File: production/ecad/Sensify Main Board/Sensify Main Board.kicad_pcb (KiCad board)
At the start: 4 copper layers, 150 parts, among them J1 1-2834011-3, J2 1-2834011-2, J3 1332645, J4 0532611271, J5 Screw_Terminal_01x08, J6 Conn_01x02_Socket, J7 Conn_01x02_Socket, J8 Conn_01x02_Socket, J9 Conn_01x02_Socket, Q1 2N700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

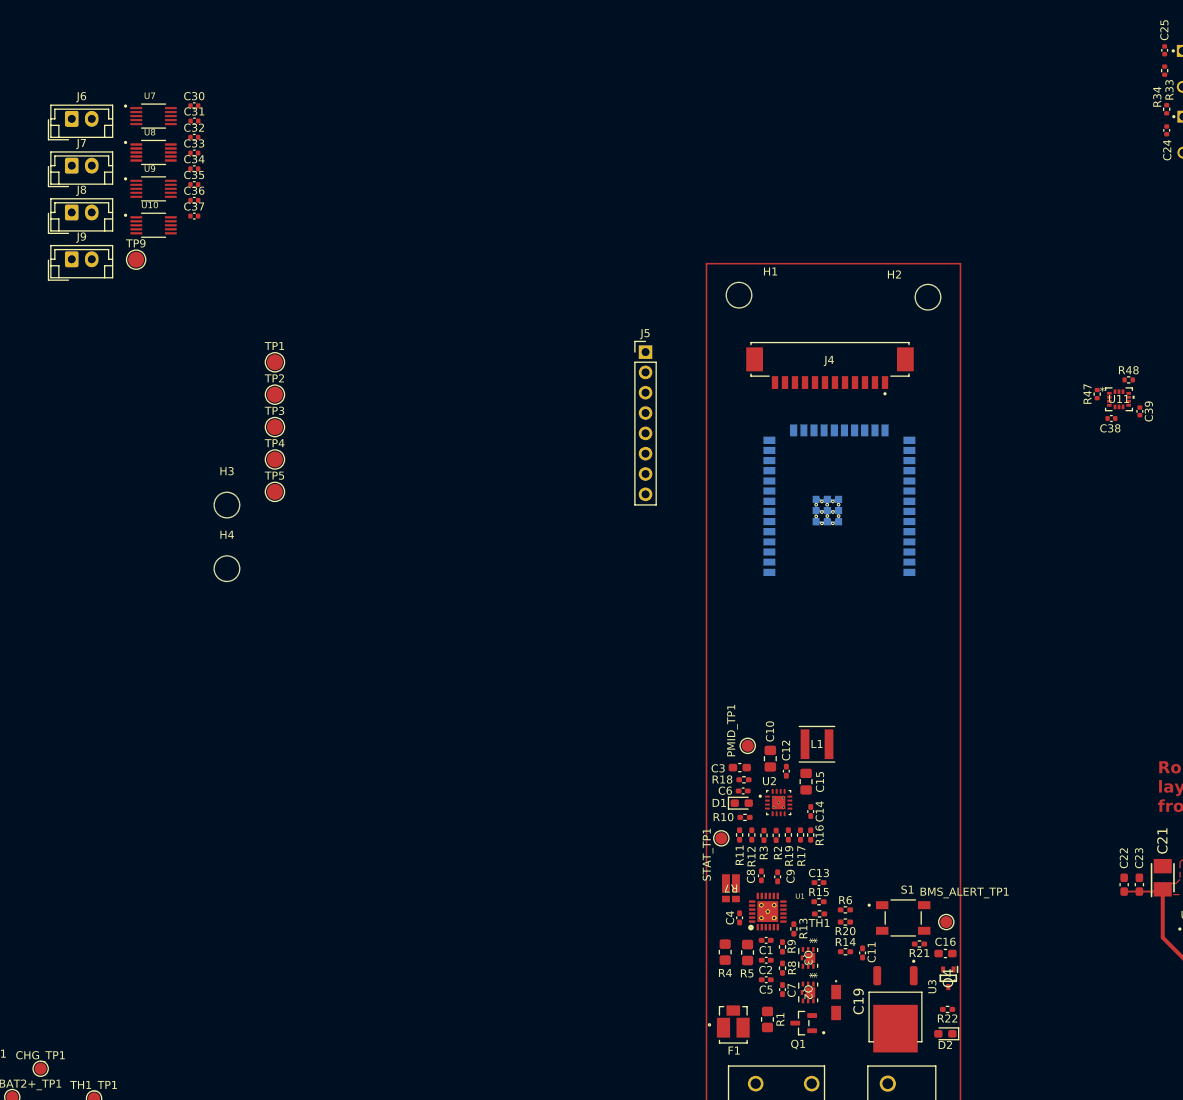
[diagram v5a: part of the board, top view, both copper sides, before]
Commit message: main board
routed haptics, modified 3.3V supply
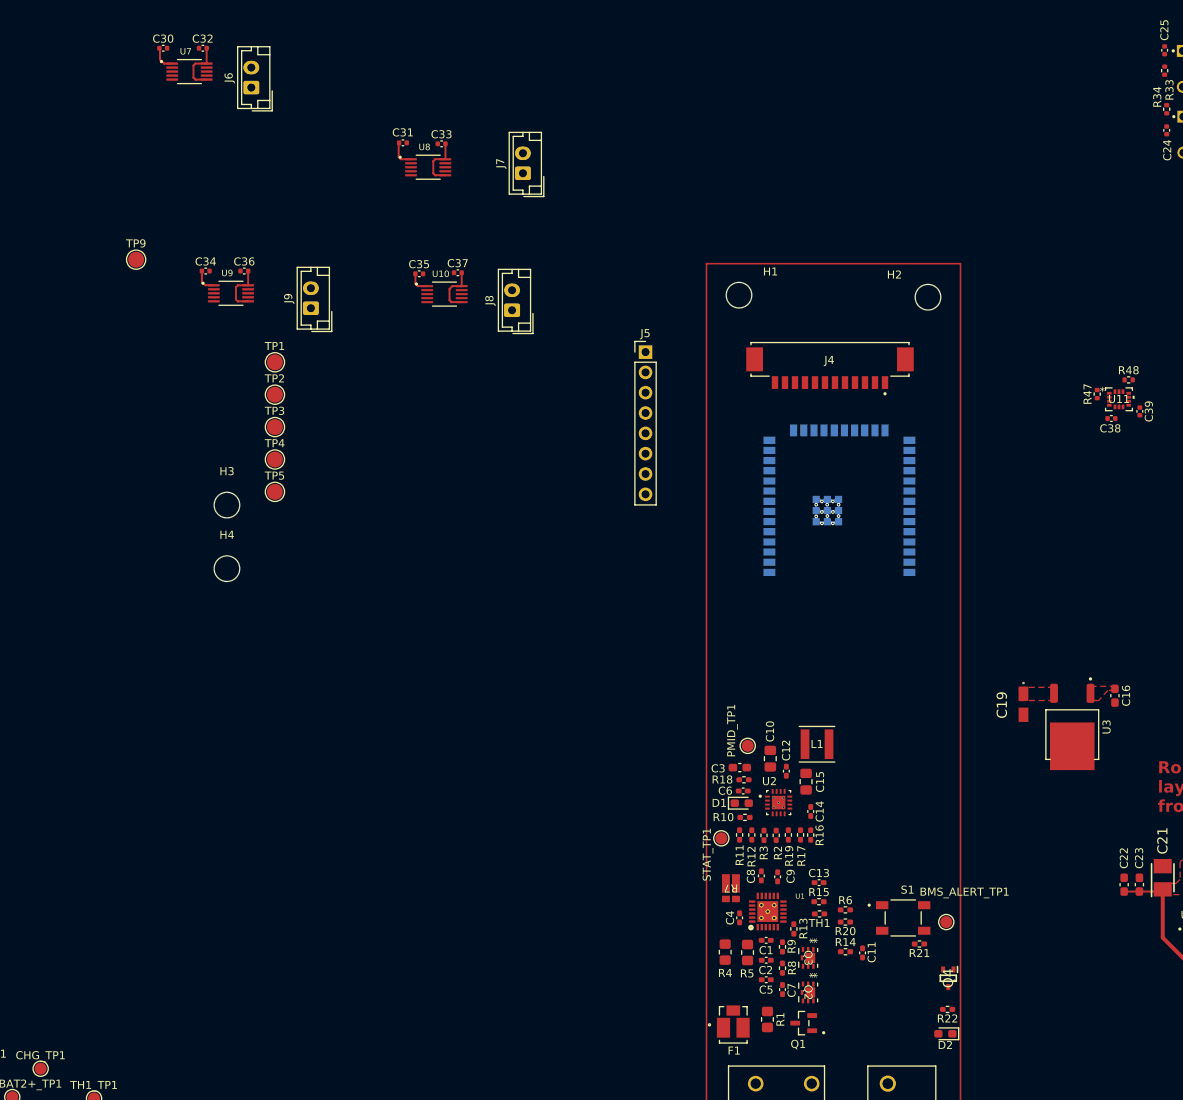
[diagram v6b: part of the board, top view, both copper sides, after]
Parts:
- moved J7 56.4 mm to (104.6, 58.3), turned to 90 degrees
- moved J8 56.4 mm to (103.2, 75.4), turned to 90 degrees
- moved C19 44.0 mm to (167.1, 124.7)
- moved U3 41.6 mm to (173.2, 127.5)
- moved C16 38.6 mm to (178.6, 123.6), turned to -90 degrees
- moved U10 37.4 mm to (94.8, 73.4)
- moved U8 34.4 mm to (92.7, 57.5)
- moved C37 33.7 mm to (96.4, 70.7)
- moved C33 30.9 mm to (94.4, 54.6)
- moved J9 30.5 mm to (78.1, 75.2), turned to 90 degrees
- moved C35 30.3 mm to (91.6, 70.9)
- moved C31 26.2 mm to (89.6, 54.5)
- moved J6 22.8 mm to (70.6, 47.6), turned to 90 degrees
- moved U9 16.2 mm to (68.1, 73.3)
- moved C34 12.9 mm to (64.9, 70.5)
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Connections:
- C30 pad 2: Earth -> GND
- C31 pad 2: Earth -> GND
- C32 pad 1: Earth -> GND
- C33 pad 1: Earth -> GND
- C34 pad 2: Earth -> GND
- C35 pad 2: Earth -> GND
- C36 pad 1: Earth -> GND
- C37 pad 1: Earth -> GND
- U10 pad 4: Earth -> GND
- U10 pad 8: Earth -> GND
- U7 pad 4: Earth -> GND
- U7 pad 8: Earth -> GND
- U8 pad 4: Earth -> GND
- U8 pad 8: Earth -> GND
- U9 pad 4: Earth -> GND
- U9 pad 8: Earth -> GND
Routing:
- net +5V: track 15.6 -> 42.2 mm
- net Net-(U8-REG): track 0.00 -> 3.46 mm
- net Net-(U7-REG): track 0.00 -> 3.17 mm
- net Net-(U9-REG): track 0.00 -> 3.00 mm
- net Net-(U10-REG): track 0.00 -> 2.82 mm
- added copper zone on F.Cu, net +3V3

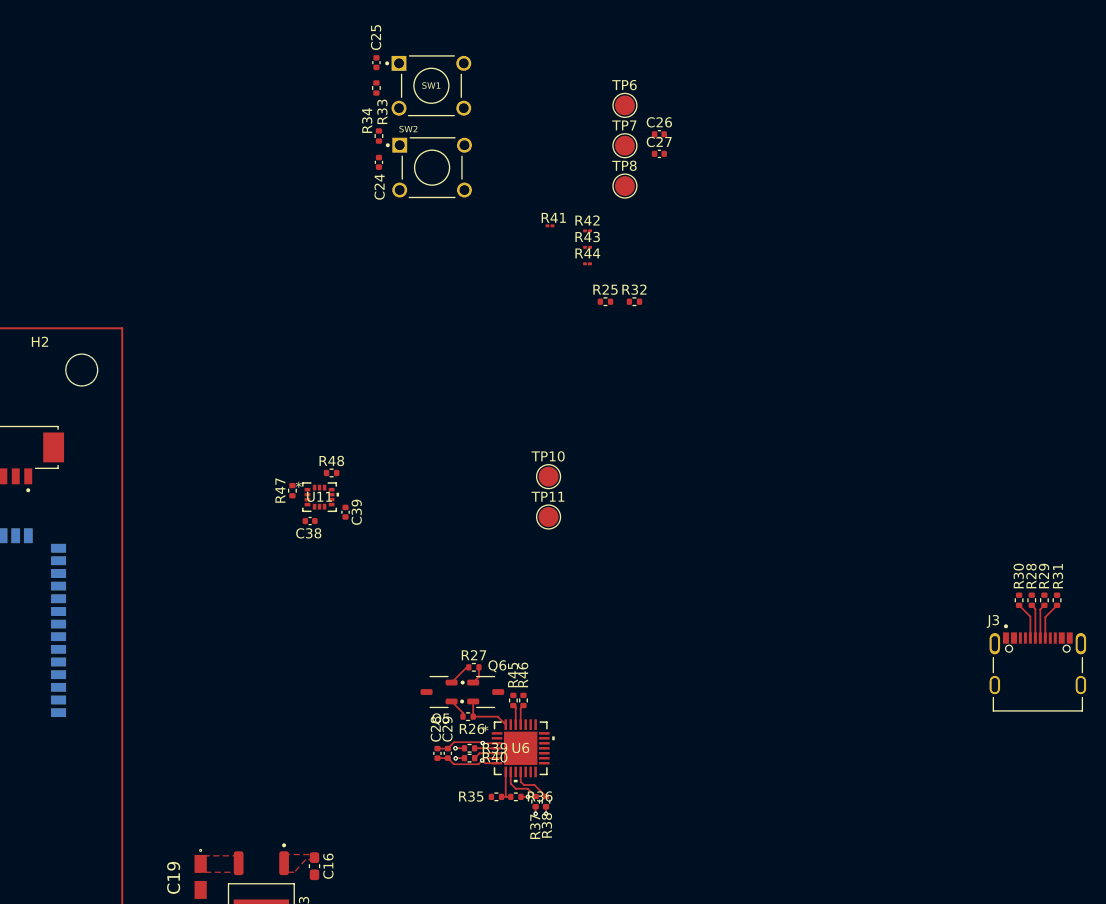
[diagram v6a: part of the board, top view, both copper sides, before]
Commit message: Finished USB to UART Routing
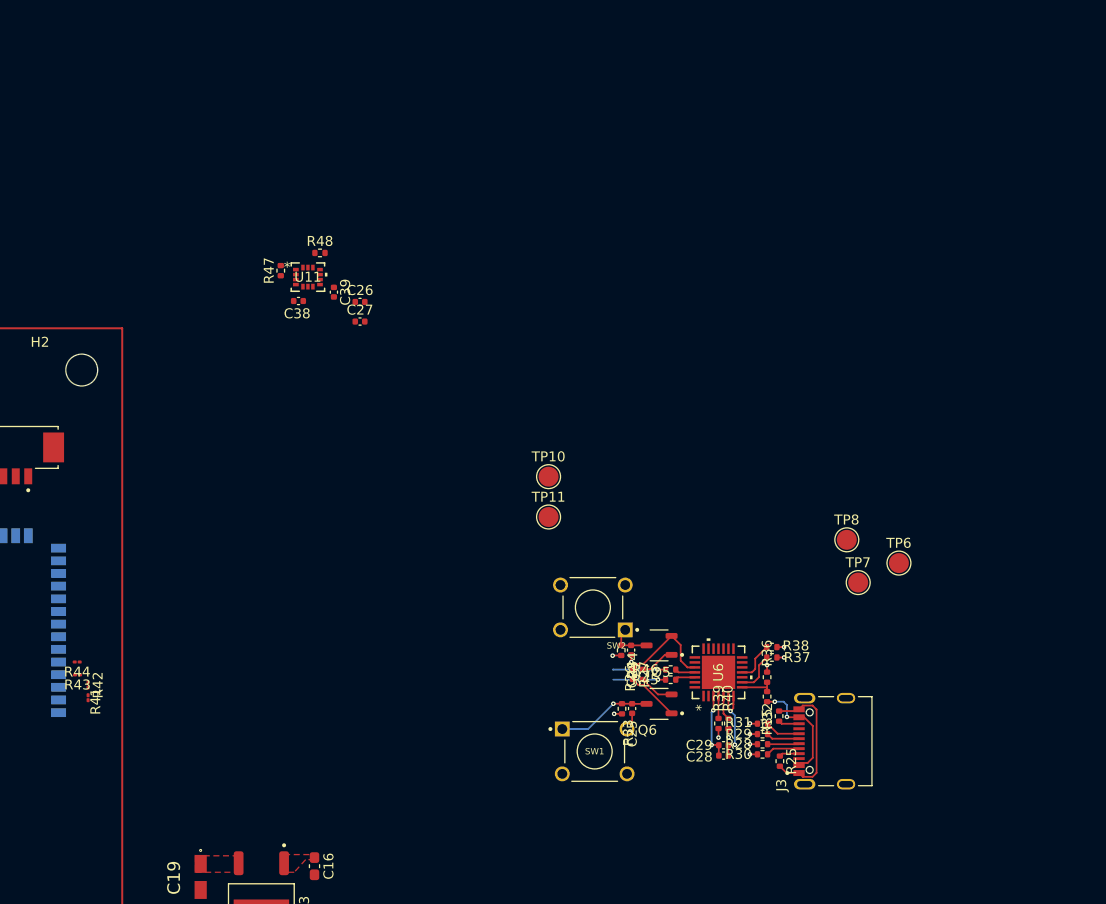
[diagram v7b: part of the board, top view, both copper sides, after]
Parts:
- moved C25 69.7 mm to (210.4, 107.8), turned to -90 degrees
- moved SW1 68.8 mm to (206.7, 112.1)
- moved R42 67.8 mm to (155.8, 105.4), turned to -90 degrees
- moved R33 67.0 mm to (209.4, 107.8)
- moved R43 66.8 mm to (154.8, 104.4), turned to 180 degrees
- moved R41 66.3 mm to (155.8, 106.7), turned to -90 degrees
- moved R44 65.0 mm to (154.7, 103.1), turned to 180 degrees
- moved R34 57.1 mm to (209.4, 101.9), turned to 90 degrees
- moved C24 55.1 mm to (210.3, 101.9)
- moved TP6 53.6 mm to (237.2, 93.2)
- moved TP7 49.7 mm to (233.1, 95.1)
- moved R25 49.3 mm to (225.3, 113.1), turned to -90 degrees
- moved SW2 47.0 mm to (206.5, 97.6), turned to 180 degrees
- moved R32 44.1 mm to (225.2, 108.5), turned to 90 degrees
- moved TP8 41.9 mm to (232.0, 90.8)
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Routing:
- net GND: track 25.7 -> 43.5 mm, vias 15 -> 17
- net FLASHING_VBUS_5V: track 0.00 -> 11.2 mm, vias 0 -> 2
- net IO0: track 0.00 -> 9.52 mm, vias 0 -> 1
- net RTS: track 2.36 -> 9.83 mm
- net UART_RXD: track 0.00 -> 5.28 mm, vias 0 -> 1
- net UART_TXD: track 0.00 -> 5.25 mm, vias 0 -> 1
- net EN: track 0.00 -> 4.27 mm
- net Net-(Q6-Pad1): track 1.77 -> 5.30 mm
- net Net-(J3-CC2): track 0.00 -> 2.11 mm
- net +3V3: track 8.80 -> 10.9 mm, vias 2 -> 5
- net Net-(J3-CC1): track 0.00 -> 2.03 mm
- net DTR: track 5.13 -> 3.49 mm
- net USB_D+: track 0.91 -> 2.44 mm, vias 1 -> 3
- net USB_D-: track 0.90 -> 2.41 mm, vias 1 -> 3
- net Net-(Q5-Pad1): track 2.00 -> 3.47 mm

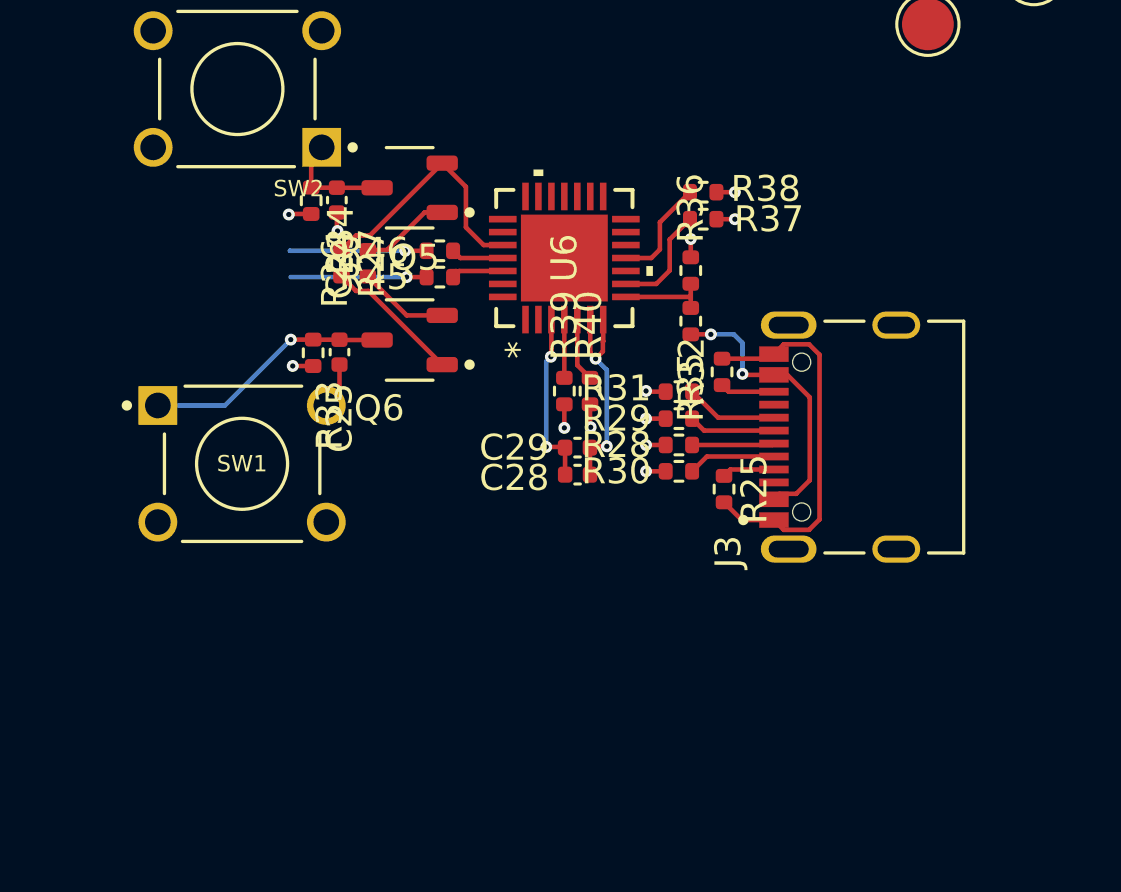
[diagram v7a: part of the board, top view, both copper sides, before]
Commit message: Deleted routing for USB to UART to allow more flexibility
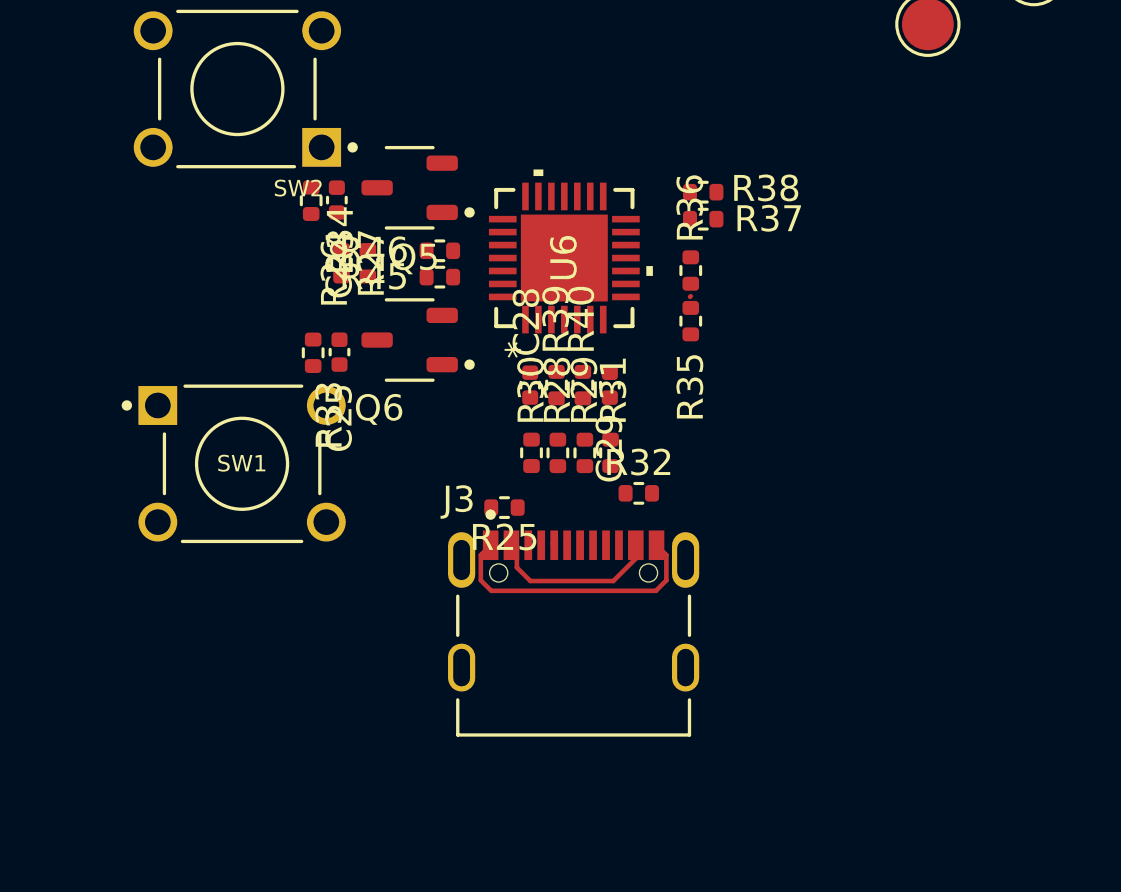
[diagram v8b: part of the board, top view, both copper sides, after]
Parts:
- moved J3 20.7 mm to (215.0, 122.5), turned to 0 degrees
- moved R25 8.50 mm to (216.8, 113.8), turned to 180 degrees
- moved R30 5.73 mm to (217.9, 111.7), turned to -90 degrees
- moved R32 5.68 mm to (222.0, 113.2), turned to 0 degrees
- moved R28 4.68 mm to (218.9, 111.7), turned to 90 degrees
- moved C28 3.91 mm to (217.8, 109.0), turned to 90 degrees
- moved R29 3.86 mm to (219.9, 111.7), turned to 90 degrees
- moved R31 3.54 mm to (220.9, 111.7), turned to -90 degrees
- moved C29 2.71 mm to (220.9, 109.0), turned to -90 degrees
- moved R39 0.38 mm to (218.8, 109.0)
- moved R40 0.36 mm to (219.8, 109.0)
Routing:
- net GND: track 43.5 -> 29.2 mm, vias 17 -> 12
- net +3V3: track 10.9 -> 0.18 mm, vias 5 -> 0
- net RTS: track 9.83 -> 0.00 mm
- net IO0: track 9.52 -> 0.03 mm, vias 1 -> 0
- net Net-(Q6-Pad1): track 5.30 -> 0.00 mm
- net UART_RXD: track 5.28 -> 0.00 mm, vias 1 -> 0
- net UART_TXD: track 5.25 -> 0.00 mm, vias 1 -> 0
- net FLASHING_VBUS_5V: track 11.2 -> 6.65 mm, vias 2 -> 0
- net Net-(U6-RSTb): track 4.21 -> 0.00 mm
- net Net-(U6-SUSPENDb): track 4.14 -> 0.00 mm
- net EN: track 4.27 -> 0.59 mm
- net Net-(J3-DP2): track 3.57 -> 0.00 mm
- net DTR: track 3.49 -> 0.00 mm
- net Net-(Q5-Pad1): track 3.47 -> 0.00 mm
- net Net-(U6-VBUS): track 3.45 -> 0.04 mm
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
